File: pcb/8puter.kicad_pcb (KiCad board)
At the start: 2 copper layers, 41 parts, among them J1 PWR-DC, SW1 RESET_SW, U1 74AC00, U2 74HC74, U3 DS1135Z, U6 MAX811MEUS-T

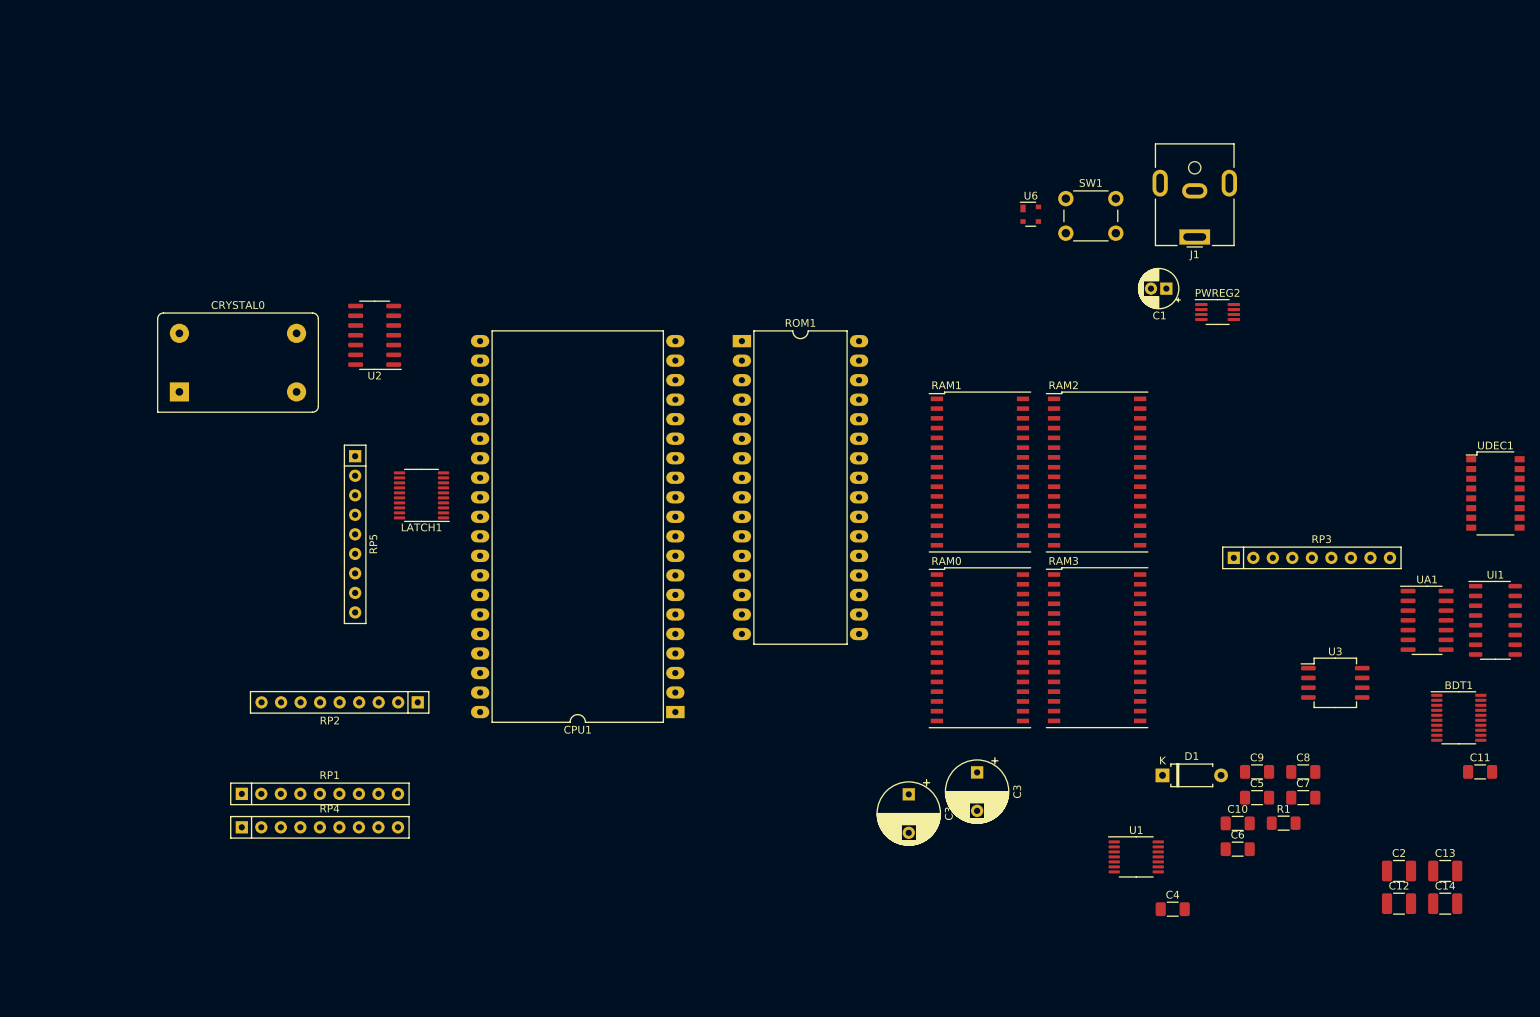
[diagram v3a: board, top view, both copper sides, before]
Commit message: Board layout, addr bus
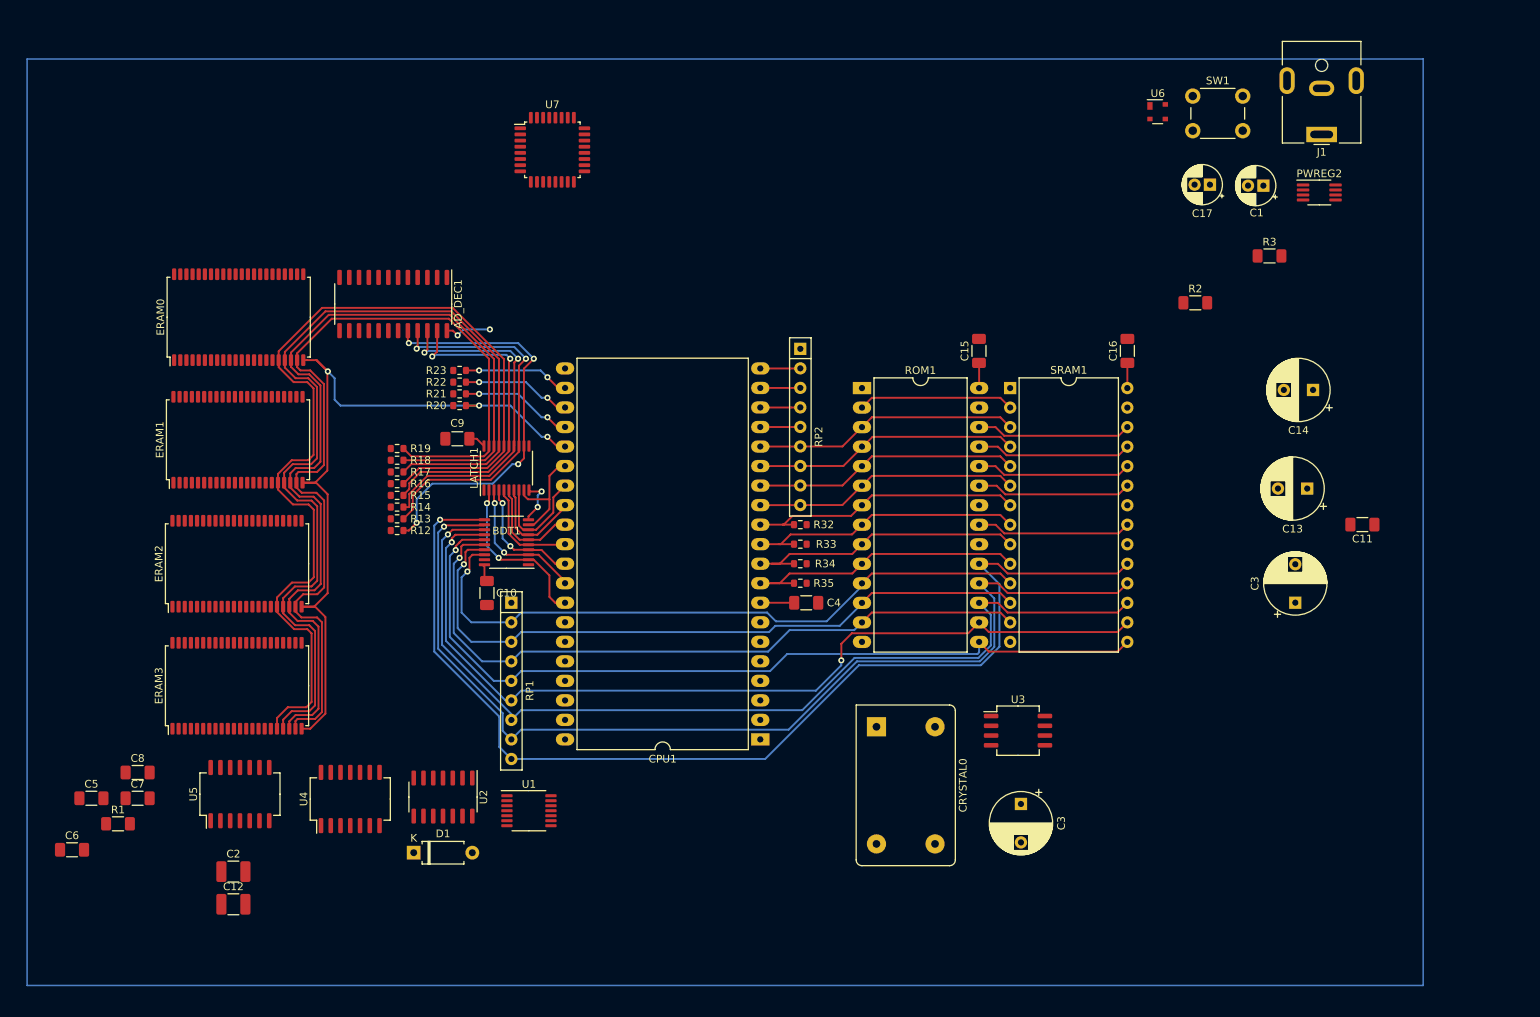
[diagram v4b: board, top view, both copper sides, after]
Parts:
- removed RAM0, RAM1, RAM2, RAM3: IS61C5128AS-25TLI, Package_SO:TSOP-II-32_21.0x10.2mm_P1.27mm
- removed RP3, RP4, RP5: 1K, Resistor_THT:R_Array_SIP9
- removed UA1: ~, Package_SO:SO-14_3.9x8.65mm_P1.27mm
- removed UDEC1: 74HC237, Package_SO:SOP-16_4.4x10.4mm_P1.27mm
- removed UI1: ~, Package_SO:SO-16_3.9x9.9mm_P1.27mm
- added AD_DEC1: 74HCT154, Package_SO:SO-24_5.3x15mm_P1.27mm, F.Cu at (105.5, 65.0)
- added C15: 100nF, Capacitor_SMD:C_1206_3216Metric_Pad1.33x1.80mm_HandSolder, F.Cu at (181.7, 71.1)
- added C16: 100nF, Capacitor_SMD:C_1206_3216Metric_Pad1.33x1.80mm_HandSolder, F.Cu at (201.0, 71.1)
- added C17: 10uF, Capacitor_THT:CP_Radial_D5.0mm_P2.00mm, F.Cu at (211.8, 49.5)
- added ERAM0: IS62WV10248, Package_SO:TSOP-II-44_10.16x18.41mm_P0.8mm, F.Cu at (85.4, 66.7)
- added ERAM1: IS62WV10248, Package_SO:TSOP-II-44_10.16x18.41mm_P0.8mm, F.Cu at (85.3, 82.7)
- added ERAM2: IS62WV10248, Package_SO:TSOP-II-44_10.16x18.41mm_P0.8mm, F.Cu at (85.2, 98.8)
- added ERAM3: IS62WV10248, Package_SO:TSOP-II-44_10.16x18.41mm_P0.8mm, F.Cu at (85.2, 114.7)
- added R12: 1K, Resistor_SMD:R_0603_1608Metric, F.Cu at (106.0, 94.5)
- added R13: 1K, Resistor_SMD:R_0603_1608Metric, F.Cu at (106.0, 93.0)
- added R14: 1K, Resistor_SMD:R_0603_1608Metric, F.Cu at (106.0, 91.4)
- added R15: 1K, Resistor_SMD:R_0603_1608Metric, F.Cu at (106.0, 89.9)
- added R16: 1K, Resistor_SMD:R_0603_1608Metric, F.Cu at (106.0, 88.4)
- added R17: 1K, Resistor_SMD:R_0603_1608Metric, F.Cu at (106.0, 86.9)
- added R18: 1K, Resistor_SMD:R_0603_1608Metric, F.Cu at (106.0, 85.3)
- added R19: 1K, Resistor_SMD:R_0603_1608Metric, F.Cu at (106.0, 83.8)
- added R2: 10K, Resistor_SMD:R_1206_3216Metric_Pad1.30x1.75mm_HandSolder, F.Cu at (209.9, 64.9)
- added R20: 1K, Resistor_SMD:R_0603_1608Metric, F.Cu at (114.2, 78.2)
- added R21: 1K, Resistor_SMD:R_0603_1608Metric, F.Cu at (114.2, 76.7)
- added R22: 1K, Resistor_SMD:R_0603_1608Metric, F.Cu at (114.2, 75.2)
- added R23: 1K, Resistor_SMD:R_0603_1608Metric, F.Cu at (114.2, 73.7)
- added R3: 10K, Resistor_SMD:R_1206_3216Metric_Pad1.30x1.75mm_HandSolder, F.Cu at (219.5, 58.8)
- added R32: 1K, Resistor_SMD:R_0603_1608Metric, F.Cu at (158.5, 93.7)
- added R33: 1K, Resistor_SMD:R_0603_1608Metric, F.Cu at (158.5, 96.3)
- added R34: 1K, Resistor_SMD:R_0603_1608Metric, F.Cu at (158.5, 98.8)
- added R35: 1K, Resistor_SMD:R_0603_1608Metric, F.Cu at (158.5, 101.3)
- added SRAM1: KM62256CLP, Package_DIP:DIP-28_W15.24mm, F.Cu at (185.8, 76.0)
- added U4: 74HC32, Package_SO:SO-14_5.3x10.2mm_P1.27mm, F.Cu at (99.9, 129.4)
- added U5: 74HC11, Package_SO:SO-14_5.3x10.2mm_P1.27mm, F.Cu at (85.6, 128.8)
- added U7: STM8S003K3T, Package_QFP:LQFP-32_7x7mm_P0.8mm, F.Cu at (126.2, 45.0)
- C13, C14: footprint Capacitor_SMD:C_1210_3225Metric_Pad1.33x2.70mm_HandSolder -> Capacitor_THT:CP_Radial_D8.0mm_P3.80mm
- R1: value ~ -> 1K
- ROM1: value SST39SF010 -> AT28HC256; footprint Package_DIP:DIP-32_W15.24mm_LongPads -> Package_DIP:DIP-28_W15.24mm_LongPads
- moved R1 151.6 mm to (69.7, 132.6)
- moved C12 151.6 mm to (84.7, 143.1)
- moved C2 151.6 mm to (84.7, 138.9)
- moved C5 151.6 mm to (66.3, 129.3)
- moved C6 151.6 mm to (63.8, 136.0)
- moved C7 151.6 mm to (72.3, 129.3)
- moved C8 151.6 mm to (72.3, 126.0)
- moved BDT1 126.0 mm to (120.3, 96.0), turned to 180 degrees
- moved C9 112.7 mm to (113.9, 82.5), turned to 180 degrees
- moved C10 102.2 mm to (117.7, 102.6), turned to -90 degrees
- moved CRYSTAL0 100.6 mm to (168.4, 120.0), turned to -90 degrees
- moved D1 97.9 mm to (108.2, 136.4)
- moved U1 79.2 mm to (123.2, 130.9)
- moved C14 69.0 mm to (225.2, 76.2), turned to 180 degrees
- moved RP2 67.8 mm to (158.5, 70.9), turned to -90 degrees
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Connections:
- net /Bus Control/LATCH_~{OE} renamed Net-(LATCH1-Pad1)
- net Net-(U2-Pad12) renamed ~{CLOCK}
- BDT1 pad 1: R/~{W} -> W~{R}
- BDT1 pad 19: /Bus Control/BUS_IN_EN -> /Bus Control/DATA_BUS_EN
- CPU1 pad 34: R/~{W} -> CPU_R~{W}
- CPU1 pad 39: unconnected-(CPU1-Pad39) -> VDA
- CPU1 pad 7: unconnected-(CPU1-Pad7) -> VPA
- LATCH1 pad 11: /Bus Control/LATCH_~{Load} -> Net-(LATCH1-Pad11)
- ROM1 pad 1: unconnected-(ROM1-Pad1) -> ADDR14
- ROM1 pad 10: ADDR2 -> ADDR0
- ROM1 pad 11: ADDR1 -> DATA0
- ROM1 pad 12: ADDR0 -> DATA1
- ROM1 pad 13: DATA0 -> DATA2
- ROM1 pad 14: DATA1 -> GND
- ROM1 pad 15: DATA2 -> DATA3
- ROM1 pad 16: GND -> DATA4
- ROM1 pad 17: DATA3 -> DATA5
- ROM1 pad 18: DATA4 -> DATA6
- ROM1 pad 19: DATA5 -> DATA7
- ROM1 pad 2: /Memory Unit/CROM_EN -> ADDR12
- ROM1 pad 20: DATA6 -> /Memory Unit/~{ROM_CS}
- ROM1 pad 21: DATA7 -> ADDR10
- ROM1 pad 22: /Memory Unit/ROM_EN -> W~{R}
- ROM1 pad 23: ADDR10 -> ADDR11
- ROM1 pad 24: R/~{W} -> ADDR9
- ROM1 pad 25: ADDR11 -> ADDR8
- ROM1 pad 26: ADDR9 -> ADDR13
- ROM1 pad 27: ADDR8 -> Net-(R2-Pad2)
- ROM1 pad 28: ADDR13 -> +5V
- ROM1 pad 3: ADDR15 -> ADDR7
- ROM1 pad 4: ADDR12 -> ADDR6
- ROM1 pad 5: ADDR7 -> ADDR5
- ROM1 pad 6: ADDR6 -> ADDR4
- ROM1 pad 7: ADDR5 -> ADDR3
- ROM1 pad 8: ADDR4 -> ADDR2
- ROM1 pad 9: ADDR3 -> ADDR1
- RP2 pad 2: /DBA0 -> ADDR11
- RP2 pad 3: /DBA1 -> ADDR10
- RP2 pad 4: /DBA2 -> ADDR9
- RP2 pad 5: /DBA3 -> ADDR8
- RP2 pad 6: /DBA4 -> ADDR7
- RP2 pad 7: /DBA5 -> ADDR6
- RP2 pad 8: /DBA6 -> ADDR5
- RP2 pad 9: /DBA7 -> ADDR4
- U1 pad 1: (no net) -> CPU_R~{W}
- U1 pad 2: (no net) -> CPU_R~{W}
- U1 pad 3: (no net) -> W~{R}
- U2 pad 2: /Bus Control/READY_IN -> Net-(R3-Pad2)
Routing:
- net DATA7: track 0.00 -> 143.1 mm, vias 0 -> 1
- net DATA6: track 0.00 -> 134.5 mm, vias 0 -> 1
- net ADDR19: track 0.00 -> 128.9 mm
- net DATA5: track 0.00 -> 126.1 mm, vias 0 -> 1
- net ADDR18: track 0.00 -> 124.8 mm
- net ADDR17: track 0.00 -> 120.6 mm
- net ADDR16: track 0.00 -> 117.3 mm
- net DATA4: track 0.00 -> 116.8 mm, vias 0 -> 2
- net DATA3: track 0.00 -> 110.6 mm, vias 0 -> 1
- net ADDR15: track 0.00 -> 101.9 mm, vias 0 -> 3
- net DATA2: track 0.00 -> 91.9 mm, vias 0 -> 1
- net DATA1: track 0.00 -> 88.8 mm, vias 0 -> 1
- net DATA0: track 0.00 -> 85.9 mm, vias 0 -> 1
- net ADDR23: track 0.00 -> 53.6 mm, vias 0 -> 4
- net ADDR22: track 0.00 -> 49.5 mm, vias 0 -> 2
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
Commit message: More routing, USB iface
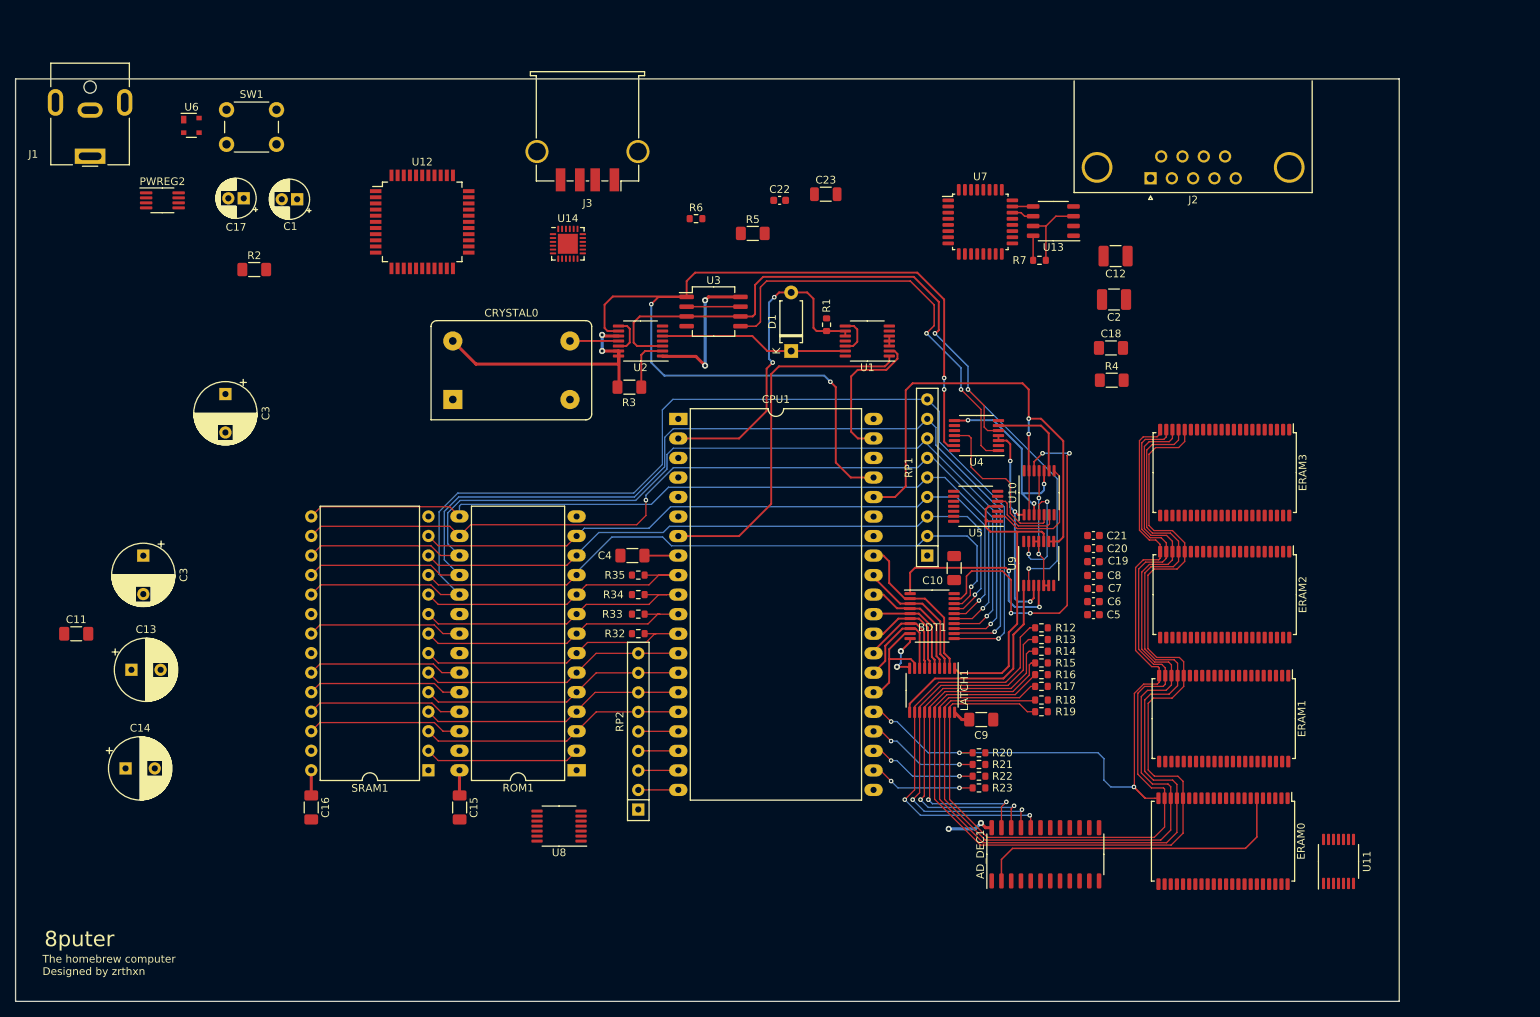
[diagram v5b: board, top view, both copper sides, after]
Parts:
- added C18: 100nF, Capacitor_SMD:C_1206_3216Metric_Pad1.33x1.80mm_HandSolder, F.Cu at (198.9, 70.7)
- added C19: 10nF, Capacitor_SMD:C_0603_1608Metric, F.Cu at (196.6, 98.5)
- added C20: 10nF, Capacitor_SMD:C_0603_1608Metric, F.Cu at (196.6, 96.8)
- added C21: 10nF, Capacitor_SMD:C_0603_1608Metric, F.Cu at (196.6, 95.1)
- added C22: 10nF, Capacitor_SMD:C_0603_1608Metric, F.Cu at (155.8, 51.5)
- added C23: 10uF, Capacitor_SMD:C_1206_3216Metric, F.Cu at (161.8, 50.7)
- added J2: DB9_Female, Connector_Dsub:DSUB-9_Female_Horizontal_P2.77x2.84mm_EdgePinOffset9.90mm_Housed_MountingHolesOffset11.32mm, F.Cu at (204.1, 48.7)
- added J3: USB_A, Connector_USB:USB_A_TE_292303-7_Horizontal, F.Cu at (130.8, 42.5)
- added R4: 10K, Resistor_SMD:R_1206_3216Metric_Pad1.30x1.75mm_HandSolder, F.Cu at (199.0, 74.9)
- added R5: 10K, Resistor_SMD:R_1206_3216Metric_Pad1.30x1.75mm_HandSolder, F.Cu at (152.3, 55.8)
- added R6: 1K, Resistor_SMD:R_0603_1608Metric, F.Cu at (144.9, 53.9)
- added R7: 1K, Resistor_SMD:R_0603_1608Metric, F.Cu at (189.6, 59.3)
- added U10: 74AC10, Package_SO:TSSOP-14_4.4x5mm_P0.65mm, F.Cu at (189.6, 89.6)
- added U11: 74AC14, Package_SO:TSSOP-14_4.4x5mm_P0.65mm, F.Cu at (228.5, 137.5)
- added U12: W65C22NxPL, Package_QFP:PQFP-44_10x10mm_P0.8mm, F.Cu at (109.3, 54.3)
- added U13: MX25V8035F, Package_SO:SOP-8_3.9x4.9mm_P1.27mm, F.Cu at (191.4, 54.2)
- added U14: FT240XQ, Package_DFN_QFN:QFN-24-1EP_4x4mm_P0.5mm_EP2.6x2.6mm, F.Cu at (128.3, 57.2)
- added U8: 74AHC00, Package_SO:TSSOP-14_4.4x5mm_P0.65mm, F.Cu at (127.1, 132.9)
- added U9: 74AHC02, Package_SO:TSSOP-14_4.4x5mm_P0.65mm, F.Cu at (189.5, 98.8)
- C5, C6, C7, C8: footprint Capacitor_SMD:C_1206_3216Metric_Pad1.33x1.80mm_HandSolder -> Capacitor_SMD:C_0603_1608Metric
- R1: footprint Resistor_SMD:R_1206_3216Metric_Pad1.30x1.75mm_HandSolder -> Resistor_SMD:R_0603_1608Metric
- U1: value 74AC00 -> 74AHC00
- U2: value 74HC74 -> 74AHC74; footprint Package_SO:SOIC-14_3.9x8.7mm_P1.27mm -> Package_SO:TSSOP-14_4.4x5mm_P0.65mm
- U4: value 74HC32 -> 74AHC32; footprint Package_SO:SO-14_5.3x10.2mm_P1.27mm -> Package_SO:TSSOP-14_4.4x5mm_P0.65mm
- U5: value 74HC11 -> 74AHC125; footprint Package_SO:SO-14_5.3x10.2mm_P1.27mm -> Package_SO:TSSOP-14_4.4x5mm_P0.65mm
- moved C11 167.9 mm to (64.3, 107.9), turned to 0 degrees
- moved C14 162.1 mm to (70.7, 125.4), turned to 0 degrees
- moved J1 160.2 mm to (66.1, 45.8)
- moved C13 154.8 mm to (71.5, 112.6), turned to 0 degrees
- moved PWREG2 150.5 mm to (75.5, 51.5)
- moved C3 150.0 mm to (73.0, 97.8), turned to -90 degrees
- moved ERAM0 145.1 mm to (213.5, 134.9), turned to -90 degrees
- moved C12 142.4 mm to (199.5, 58.8), turned to 180 degrees
- moved C6 136.7 mm to (196.6, 103.7), turned to 180 degrees
- moved C2 136.6 mm to (199.3, 64.4), turned to 180 degrees
- moved ERAM1 133.3 mm to (213.6, 119.0), turned to -90 degrees
- moved C5 132.5 mm to (196.6, 105.4), turned to 180 degrees
- moved ERAM3 131.4 mm to (213.7, 87.0), turned to -90 degrees
- moved ERAM2 128.5 mm to (213.7, 102.8), turned to -90 degrees
- moved C7 127.3 mm to (196.6, 102.0), turned to 180 degrees
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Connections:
- BDT1 pad 1: W~{R} -> Net-(BDT1-Pad1)
- CPU1 pad 3: ~{ABORT} -> Net-(CPU1-Pad3)
- ERAM0 pad 17: WRITE -> ~{WRITE}
- ERAM0 pad 40: unconnected-(ERAM0-Pad40) -> Net-(ERAM0-Pad40)
- ERAM0 pad 41: W~{R} -> ~{READ}
- ERAM1 pad 17: WRITE -> ~{WRITE}
- ERAM1 pad 40: unconnected-(ERAM1-Pad40) -> Net-(ERAM1-Pad40)
- ERAM1 pad 41: W~{R} -> ~{READ}
- ERAM2 pad 17: WRITE -> ~{WRITE}
- ERAM2 pad 40: unconnected-(ERAM2-Pad40) -> Net-(ERAM2-Pad40)
- ERAM2 pad 41: W~{R} -> ~{READ}
- ERAM3 pad 17: WRITE -> ~{WRITE}
- ERAM3 pad 40: unconnected-(ERAM3-Pad40) -> Net-(ERAM3-Pad40)
- ERAM3 pad 41: W~{R} -> ~{READ}
- LATCH1 pad 1: Net-(LATCH1-Pad1) -> /Bus Control/~{LATCH_OE}
- LATCH1 pad 11: Net-(LATCH1-Pad11) -> /Bus Control/LATCH_ADDR
- ROM1 pad 22: W~{R} -> ~{READ}
- SRAM1 pad 22: W~{R} -> ~{READ}
- SRAM1 pad 27: WRITE -> ~{WRITE}
- U1 pad 1: CPU_R~{W} -> VPA
- U1 pad 10: BE -> RDY
- U1 pad 2: CPU_R~{W} -> VDA
- U1 pad 3: W~{R} -> Net-(U1-Pad3)
- U1 pad 4: RDY -> Net-(U1-Pad3)
- U1 pad 5: RDY -> Net-(U1-Pad3)
- U1 pad 6: Net-(U1-Pad12) -> /Bus Control/BUS_OPCODE
- U1 pad 8: Net-(LATCH1-Pad1) -> Net-(U1-Pad12)
- U1 pad 9: BE -> RDY
- U2 pad 3: CLOCK -> /Bus Control/CLK=
- U2 pad 6: unconnected-(U2-Pad6) -> /Bus Control/~{RDY_R}
- U3 pad 2: unconnected-(U3-Pad2) -> /Bus Control/CLK-
- U3 pad 3: unconnected-(U3-Pad3) -> /Bus Control/CLK=
- U3 pad 5: unconnected-(U3-Pad5) -> /Bus Control/CLK+
- U3 pad 6: unconnected-(U3-Pad6) -> /Bus Control/CLK=
- U3 pad 7: Net-(U3-Pad7) -> /Bus Control/CLK-
- U4 pad 1: Net-(U4-Pad1) -> /Bus Control/CLK+
- U4 pad 11: unconnected-(U4-Pad11) -> Net-(U10-Pad5)
- U4 pad 12: +5V -> /Bus Control/~{RDY_R}
- U4 pad 13: +5V -> CLOCK
- U4 pad 2: Net-(LATCH1-Pad1) -> /Bus Control/~{RDY_R}
- U4 pad 3: /Bus Control/DATA_BUS_EN -> Net-(U10-Pad1)
- U4 pad 4: CLOCK -> Net-(U10-Pad1)
- U4 pad 5: CPU_R~{W} -> /Bus Control/CLK=
- U4 pad 6: WRITE -> Net-(U10-Pad9)
- U5 pad 1: +5V -> /Bus Control/~{LATCH_OE}
- U5 pad 10: VDA -> unconnected-(U5-Pad10)
- U5 pad 11: VDA -> unconnected-(U5-Pad11)
- U5 pad 12: Net-(U4-Pad1) -> +5V
- U5 pad 13: Net-(U3-Pad7) -> unconnected-(U5-Pad13)
- U5 pad 2: ~{CLOCK} -> Net-(U10-Pad8)
- U5 pad 3: Net-(D1-Pad1) -> ~{READ}
- U5 pad 4: ~{CLOCK} -> /Bus Control/~{LATCH_OE}
- U5 pad 5: Net-(U3-Pad7) -> Net-(U10-Pad6)
- U5 pad 6: Net-(LATCH1-Pad11) -> ~{WRITE}
- U5 pad 8: /Bus Control/BUS_OPCODE -> unconnected-(U5-Pad8)
- U5 pad 9: VPA -> +5V
- U7 pad 2: unconnected-(U7-Pad2) -> /Memory Unit/~{VID_CS}
- U7 pad 22: unconnected-(U7-Pad22) -> Net-(U13-Pad6)
- U7 pad 23: unconnected-(U7-Pad23) -> Net-(U13-Pad5)
- U7 pad 24: unconnected-(U7-Pad24) -> Net-(U13-Pad2)
- U7 pad 25: unconnected-(U7-Pad25) -> DATA0
- U7 pad 26: unconnected-(U7-Pad26) -> DATA1
- U7 pad 27: unconnected-(U7-Pad27) -> DATA2
- U7 pad 28: unconnected-(U7-Pad28) -> DATA3
- U7 pad 29: unconnected-(U7-Pad29) -> DATA4
- U7 pad 30: unconnected-(U7-Pad30) -> DATA5
- U7 pad 31: unconnected-(U7-Pad31) -> DATA6
- U7 pad 32: unconnected-(U7-Pad32) -> DATA7
- U7 pad 4: unconnected-(U7-Pad4) -> GND
- U7 pad 6: unconnected-(U7-Pad6) -> +5V
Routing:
- net CLOCK: track 0.00 -> 127.1 mm, vias 0 -> 4
- net /Bus Control/CLK=: track 0.00 -> 107.0 mm, vias 0 -> 3
- net BE: track 0.00 -> 70.6 mm, vias 0 -> 2
- net +5V: track 21.7 -> 77.5 mm, vias 2 -> 6
- net /Bus Control/CLK+: track 0.00 -> 55.7 mm, vias 0 -> 2
- net /Bus Control/DATA_BUS_EN: track 0.00 -> 48.9 mm, vias 0 -> 4
- net VPA: track 0.00 -> 47.5 mm
- net RDY: track 0.00 -> 43.0 mm, vias 0 -> 2
- net /Memory Unit/~{ERAM_CS0}: track 0.00 -> 42.3 mm
- net /Bus Control/~{LATCH_OE}: track 0.00 -> 40.3 mm
- net Net-(U10-Pad1): track 0.00 -> 28.5 mm, vias 0 -> 3
- net /Bus Control/LATCH_ADDR: track 0.00 -> 27.9 mm
- net Net-(BDT1-Pad1): track 0.00 -> 27.1 mm, vias 0 -> 2
- net VA: track 0.00 -> 25.3 mm, vias 0 -> 3
- net Net-(D1-Pad1): track 0.00 -> 24.6 mm
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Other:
- board outline added: 180 x 120 mm
- rule pad_to_mask_clearance: 0 -> 0.05
- board text added: "8puter"
- board text added: "The homebrew computer Designed by zrthxn"
